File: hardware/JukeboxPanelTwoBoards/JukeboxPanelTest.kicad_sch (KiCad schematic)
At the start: 21 parts, among them J1 Raspberry_Pi_2_3, J2 Jukebox Panel, J3 +3.3V, J4 +5V, J5 GND, J6 Display Header, J7 8P8C

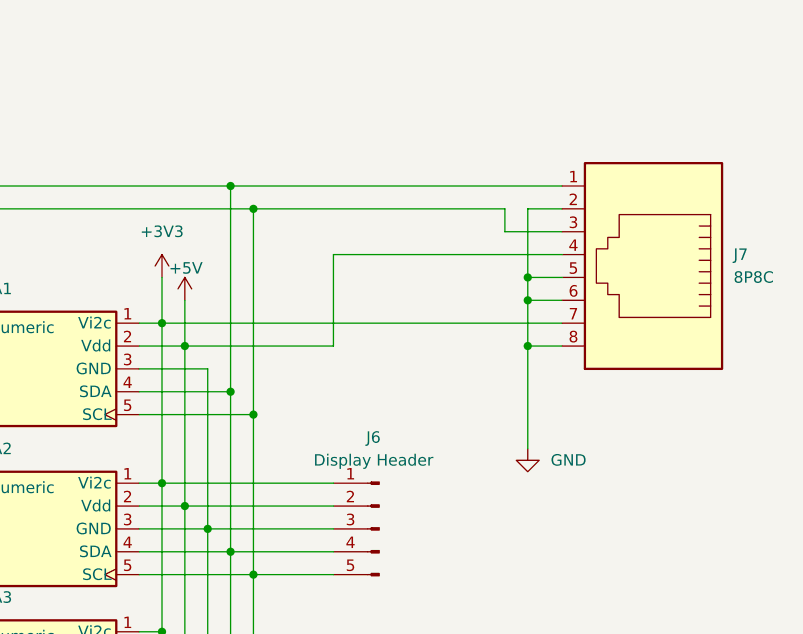
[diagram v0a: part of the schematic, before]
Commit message: Add RJ45 8P8C connector schematic for JukeboxPanelTwoBoards
This commit introduces a new schematic file for the RJ45 8P8C connector used in the JukeboxPanelTwoBoards project. The schematic includes detailed properties, pin configurations, and global labels for power and signal connections. This addition enhances the project's documentation and supports future development and assembly processes.
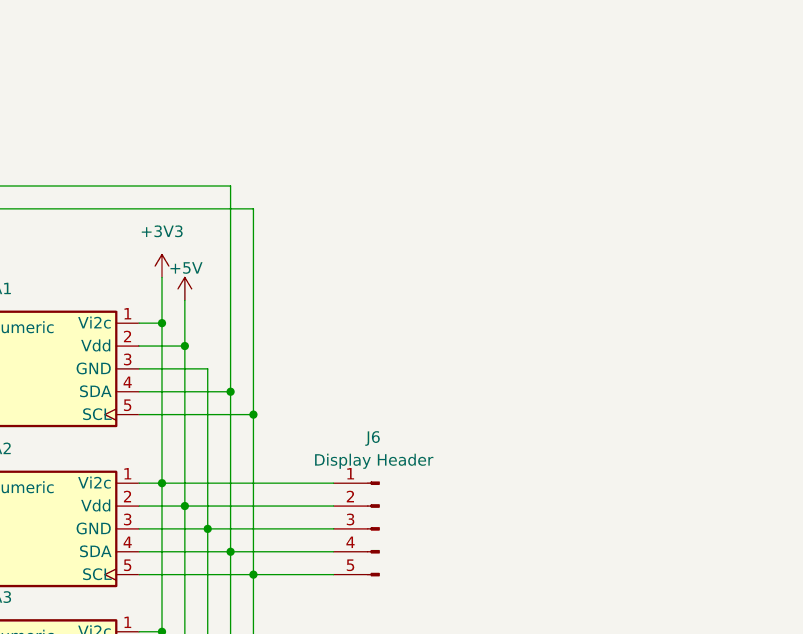
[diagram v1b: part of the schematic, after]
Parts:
- removed J7: 8P8C, Connector_RJ:RJ45_Ninigi_GE, symbol Connector:8P8C
